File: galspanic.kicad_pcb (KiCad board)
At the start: 2 copper layers, 50 x 150 mm, 21 parts, among them J1 x68000_expansion, U1 CY62167E, U2 CY62167E, U3 CY62167E, U4 CY62167E, U5 CY62167E, U6 ATF22V10C-10XU

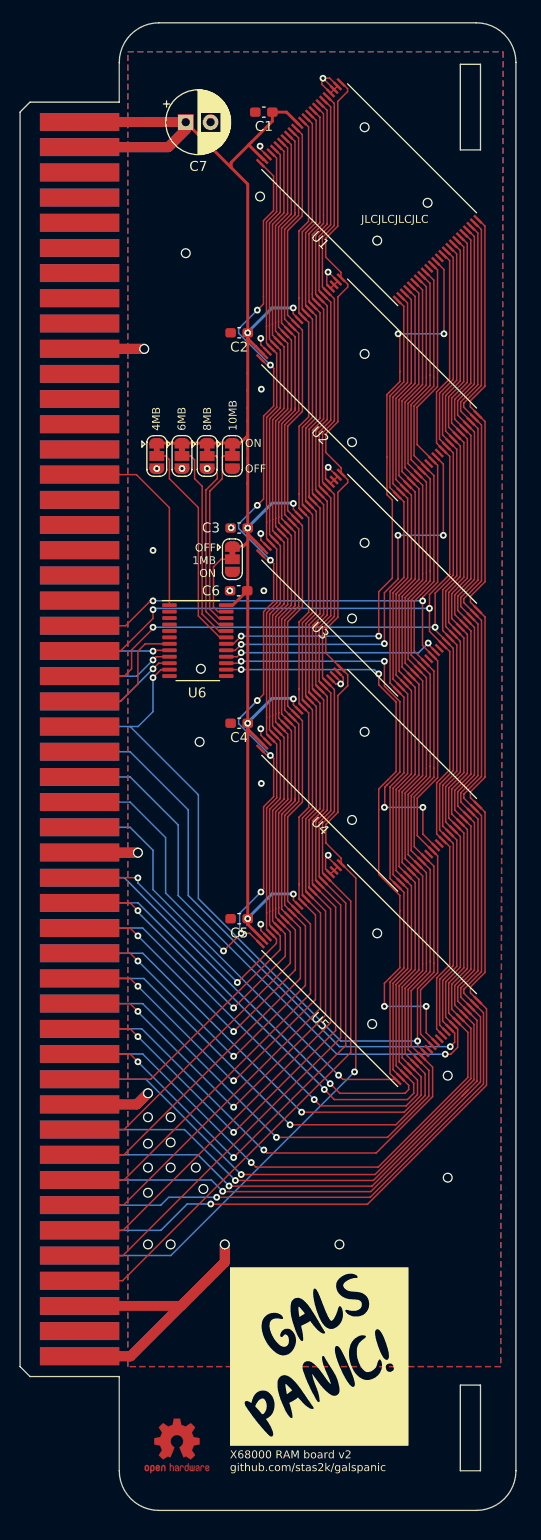
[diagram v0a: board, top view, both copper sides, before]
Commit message: Small Update
Added LCSC Part numbers
Extended Ground Plane
Replaced throughole capacitor with SMD capacitor
Removed vias on footprint pads
Changed via dimensions to 0.6/0.3
Added stitching vias
Rotated solder jumper text
Changed solder mask to black
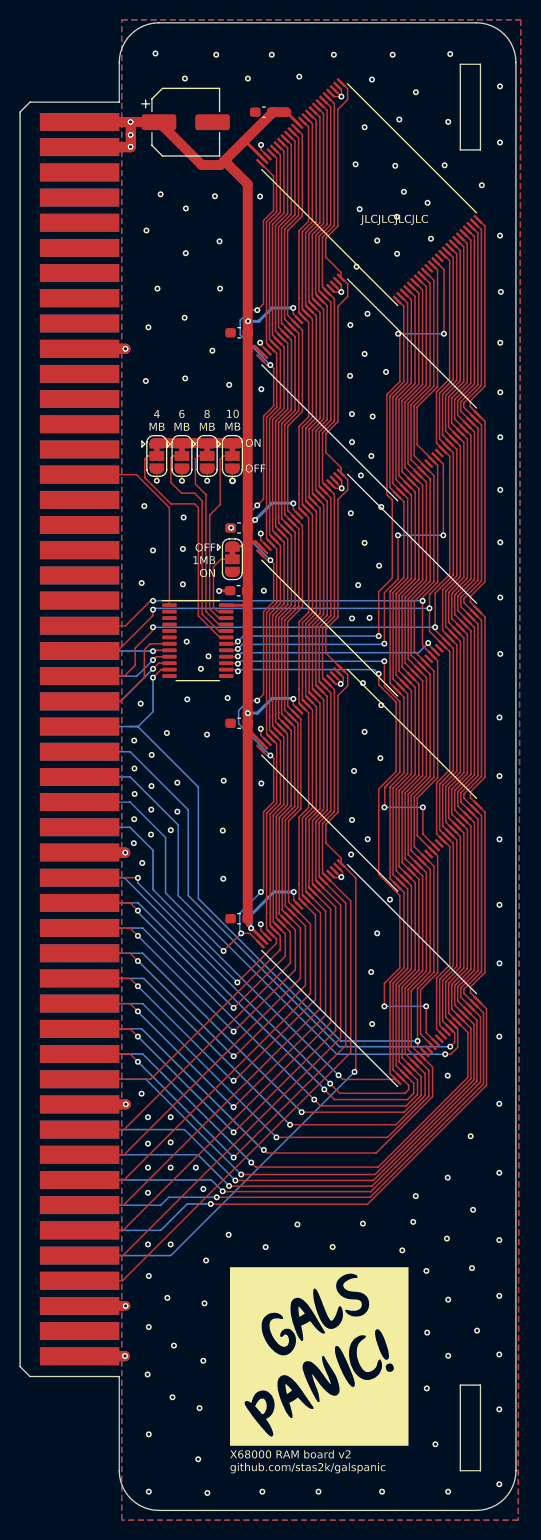
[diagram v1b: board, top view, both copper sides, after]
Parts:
- removed REF**: OSHW-Logo2_7.3x6mm_Copper, Symbol:OSHW-Logo2_7.3x6mm_Copper
- C7: footprint Capacitor_THT:CP_Radial_D6.3mm_P2.50mm -> Capacitor_SMD:CP_Elec_6.3x7.7
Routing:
- net GND: track 128.0 -> 73.3 mm, vias 52 -> 199
- net VCC: track 194.3 -> 224.1 mm, vias 8 -> 11
- net /MS4: track 22.1 -> 23.9 mm
- net /MS6: track 20.4 -> 22.1 mm
- net /A5: track 138.5 -> 137.6 mm
- net /MS10: track 19.6 -> 18.9 mm
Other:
- board text added: "10 MB"
- board text added: "4 MB"
- board text added: "6 MB"
- board text added: "8 MB"
- board text removed: "4MB 6MB 8MB 10MB"
